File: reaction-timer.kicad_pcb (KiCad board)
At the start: 2 copper layers, 48 x 80 mm, 38 parts, among them IC1 4026, IC2 4026, IC3 4026, IC5 NE555P, IC6 NE555P, IC7 NE555P

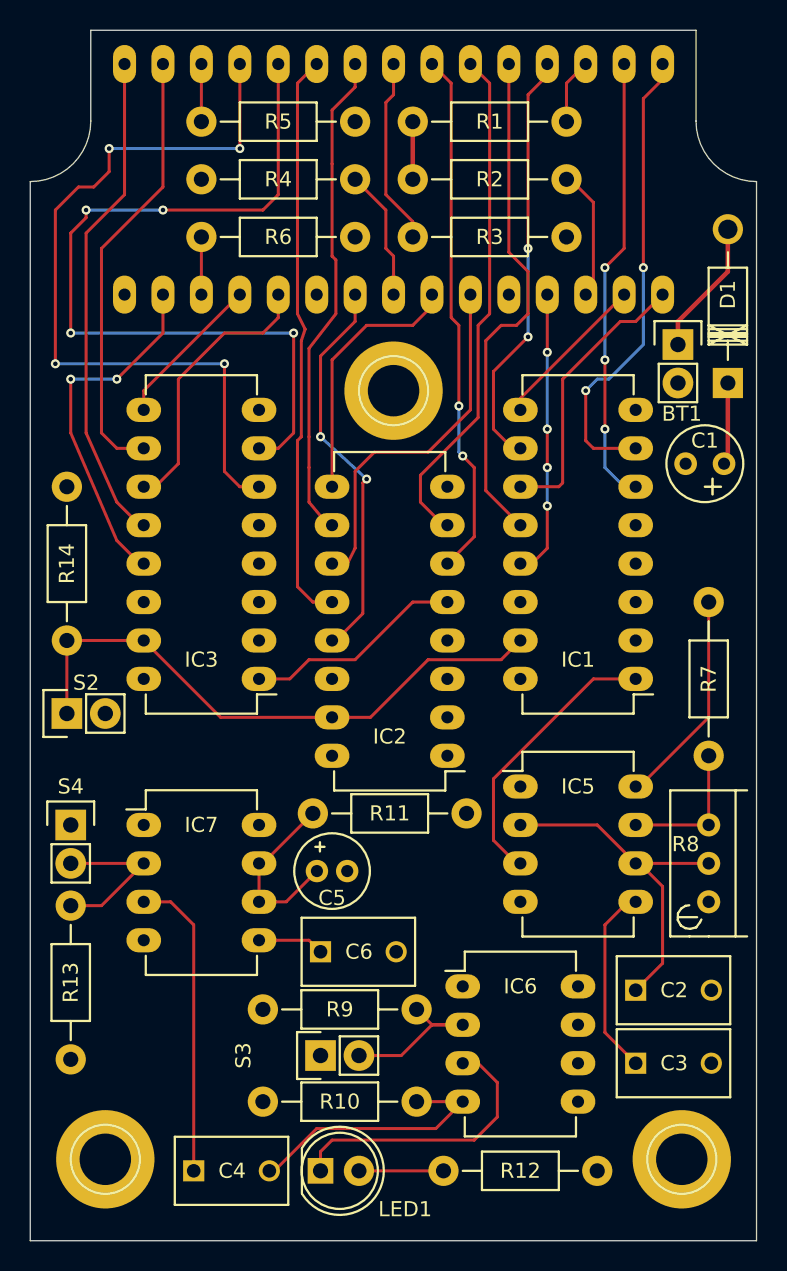
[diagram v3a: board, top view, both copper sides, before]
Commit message: Connect Vcc everywhere
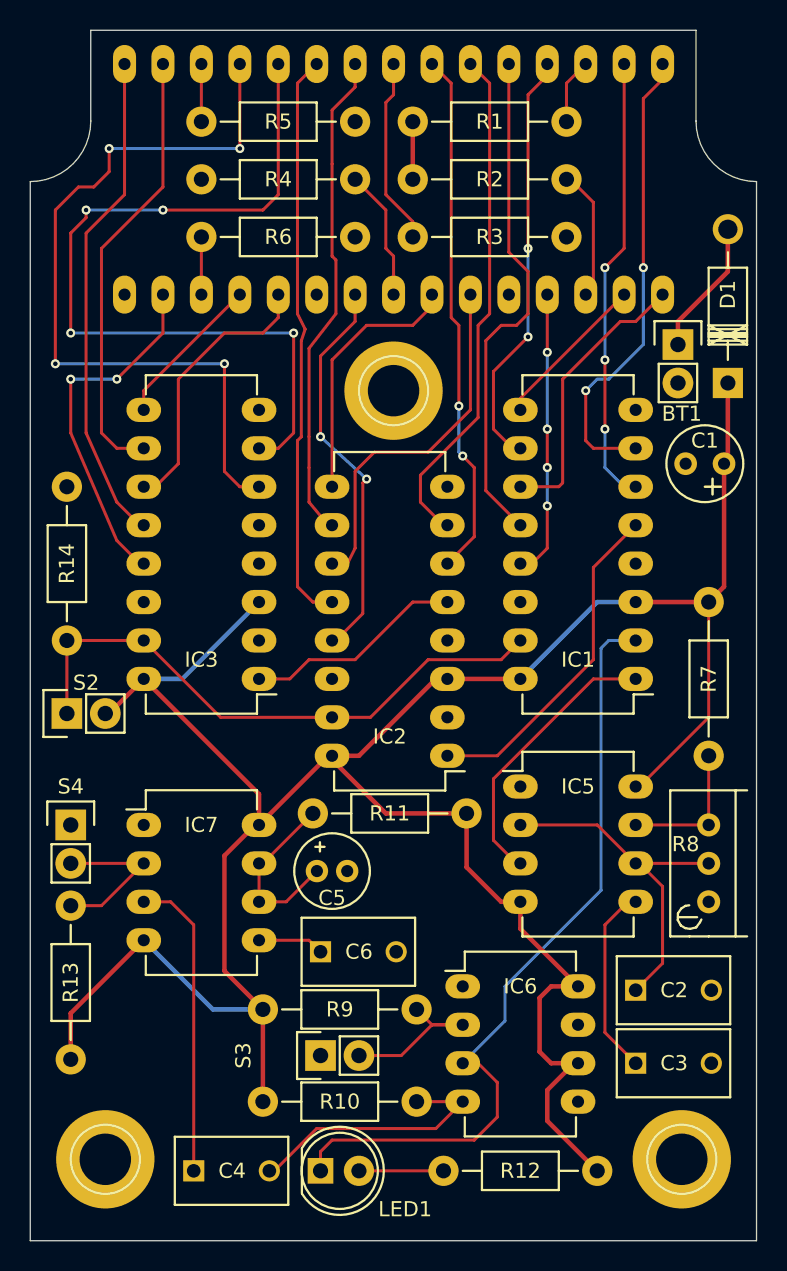
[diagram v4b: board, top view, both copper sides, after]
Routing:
- net Net-(C1-Pad1): track 19.8 -> 175.8 mm
- net Net-(IC1-Pad2): track 19.0 -> 52.7 mm
- net Net-(IC1-Pad5): track 0.00 -> 22.3 mm
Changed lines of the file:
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@@
   (general
     (links 104)
-    (no_connects 48)
+    (no_connects 28)
     (area 57.269499 61.269499 105.270501 141.270501)
     (thickness 1.6)
     (drawings 8)
-    (tracks 268)
+    (tracks 321)
     (zones 0)
     (modules 38)
@@
   (segment (start 100.076 82.042) (end 100.076 80.518) (width 0.3) (layer F.Cu) (net 31))
   (segment (start 82.55 67.31) (end 82.55 71.12) (width 0.3) (layer F.Cu) (net 32))
+  (segment (start 72.39 113.792) (end 72.136 113.792) (width 0.3) (layer F.Cu) (net 33) (status C00000))
+  (segment (start 72.136 113.792) (end 70.104 115.824) (width 0.3) (layer F.Cu) (net 33) (status 400000))
+  (segment (start 70.104 123.444) (end 72.644 125.984) (width 0.3) (layer F.Cu) (net 33) (status 800000))
+  (segment (start 70.104 115.824) (end 70.104 123.444) (width 0.3) (layer F.Cu) (net 33))
+  (segment (start 93.472 129.54) (end 93.218 129.54) (width 0.3) (layer F.Cu) (net 33) (status C00000))
+  (segment (start 93.218 129.54) (end 91.44 131.318) (width 0.3) (layer F.Cu) (net 33) (status 400000))
+  (segment (start 91.44 133.35) (end 94.742 136.652) (width 0.3) (layer F.Cu) (net 33) (status 800000))
+  (segment (start 91.44 131.318) (end 91.44 133.35) (width 0.3) (layer F.Cu) (net 33))
+  (segment (start 93.472 124.46) (end 91.694 124.46) (width 0.3) (layer F.Cu) (net 33) (status 400000))
+  (segment (start 91.694 129.54) (end 93.472 129.54) (width 0.3) (layer F.Cu) (net 33) (status 800000))
+  (segment (start 90.932 128.778) (end 91.694 129.54) (width 0.3) (layer F.Cu) (net 33))
+  (segment (start 90.932 125.222) (end 90.932 128.778) (width 0.3) (layer F.Cu) (net 33))
+  (segment (start 91.694 124.46) (end 90.932 125.222) (width 0.3) (layer F.Cu) (net 33))
+  (segment (start 89.662 118.872) (end 89.662 120.65) (width 0.3) (layer F.Cu) (net 33) (status 400000))
+  (segment (start 89.662 120.65) (end 93.472 124.46) (width 0.3) (layer F.Cu) (net 33) (status 800000))
+  (segment (start 89.662 118.872) (end 88.392 118.872) (width 0.3) (layer F.Cu) (net 33) (status 400000))
+  (segment (start 86.106 116.586) (end 86.106 113.03) (width 0.3) (layer F.Cu) (net 33) (status 800000))
+  (segment (start 88.392 118.872) (end 86.106 116.586) (width 0.3) (layer F.Cu) (net 33))
+  (segment (start 77.216 109.22) (end 77.216 109.474) (width 0.3) (layer F.Cu) (net 33) (status C00000))
+  (segment (start 77.216 109.474) (end 80.772 113.03) (width 0.3) (layer F.Cu) (net 33) (status 400000))
+  (segment (start 80.772 113.03) (end 86.106 113.03) (width 0.3) (layer F.Cu) (net 33) (status 800000))
+  (segment (start 72.644 125.984) (end 72.644 132.08) (width 0.3) (layer F.Cu) (net 33) (status C00000))
+  (segment (start 72.644 125.984) (end 69.342 125.984) (width 0.3) (layer B.Cu) (net 33) (status 400000))
+  (segment (start 69.342 125.984) (end 64.77 121.412) (width 0.3) (layer B.Cu) (net 33) (status 800000))
+  (segment (start 59.944 129.286) (end 59.944 126.238) (width 0.3) (layer F.Cu) (net 33) (status 400000))
+  (segment (start 59.944 126.238) (end 64.77 121.412) (width 0.3) (layer F.Cu) (net 33) (status 800000))
+  (segment (start 64.77 104.14) (end 67.31 104.14) (width 0.3) (layer B.Cu) (net 33) (status 400000))
+  (segment (start 67.31 104.14) (end 72.39 99.06) (width 0.3) (layer B.Cu) (net 33) (status 800000))
+  (segment (start 62.23 106.426) (end 62.484 106.426) (width 0.3) (layer F.Cu) (net 33) (status C00000))
+  (segment (start 62.484 106.426) (end 64.77 104.14) (width 0.3) (layer F.Cu) (net 33) (status C00000))
+  (segment (start 72.39 113.792) (end 72.39 111.76) (width 0.3) (layer F.Cu) (net 33) (status 400000))
+  (segment (start 72.39 111.76) (end 64.77 104.14) (width 0.3) (layer F.Cu) (net 33) (status 800000))
+  (segment (start 77.216 109.22) (end 76.962 109.22) (width 0.3) (layer F.Cu) (net 33) (status C00000))
+  (segment (start 76.962 109.22) (end 72.39 113.792) (width 0.3) (layer F.Cu) (net 33) (status C00000))
+  (segment (start 84.836 104.14) (end 84.074 104.14) (width 0.3) (layer F.Cu) (net 33) (status C00000))
+  (segment (start 84.074 104.14) (end 78.994 109.22) (width 0.3) (layer F.Cu) (net 33) (status 400000))
+  (segment (start 78.994 109.22) (end 77.216 109.22) (width 0.3) (layer F.Cu) (net 33) (status 800000))
+  (segment (start 89.662 104.14) (end 84.836 104.14) (width 0.3) (layer F.Cu) (net 33) (status C00000))
+  (segment (start 97.282 99.06) (end 94.742 99.06) (width 0.3) (layer B.Cu) (net 33) (status 400000))
+  (segment (start 94.742 99.06) (end 89.662 104.14) (width 0.3) (layer B.Cu) (net 33) (status 800000))
+  (segment (start 102.108 99.06) (end 97.282 99.06) (width 0.3) (layer F.Cu) (net 33))
+  (segment (start 103.124 89.916) (end 103.124 98.044) (width 0.3) (layer F.Cu) (net 33))
+  (segment (start 103.124 98.044) (end 102.108 99.06) (width 0.3) (layer F.Cu) (net 33))
   (segment (start 103.37546 84.582) (end 103.37546 89.66454) (width 0.3) (layer F.Cu) (net 33))
   (segment (start 102.108 106.68) (end 102.108 99.06) (width 0.2) (layer F.Cu) (net 33))
@@
   (segment (start 89.408 116.332) (end 87.884 114.808) (width 0.2) (layer F.Cu) (net 40))
   (segment (start 89.662 116.332) (end 89.408 116.332) (width 0.2) (layer F.Cu) (net 40))
+  (segment (start 97.282 101.6) (end 95.504 101.6) (width 0.2) (layer B.Cu) (net 41) (status 400000))
+  (segment (start 88.646 126.746) (end 85.852 129.54) (width 0.2) (layer B.Cu) (net 41) (status 800000))
+  (segment (start 88.646 124.46) (end 88.646 126.746) (width 0.2) (layer B.Cu) (net 41))
+  (segment (start 94.996 118.11) (end 88.646 124.46) (width 0.2) (layer B.Cu) (net 41))
+  (segment (start 94.996 102.108) (end 94.996 118.11) (width 0.2) (layer B.Cu) (net 41))
+  (segment (start 95.504 101.6) (end 94.996 102.108) (width 0.2) (layer B.Cu) (net 41))
   (segment (start 86.868 129.54) (end 85.852 129.54) (width 0.2) (layer F.Cu) (net 41))
   (segment (start 76.45266 135.38334) (end 77.216 134.62) (width 0.2) (layer F.Cu) (net 41))
@@
   (segment (start 88.138 130.81) (end 86.868 129.54) (width 0.2) (layer F.Cu) (net 41))
   (segment (start 76.45266 136.652) (end 76.45266 135.38334) (width 0.2) (layer F.Cu) (net 41))
+  (segment (start 84.836 109.22) (end 88.138 109.22) (width 0.2) (layer F.Cu) (net 42) (status 400000))
+  (segment (start 94.488 96.774) (end 97.282 93.98) (width 0.2) (layer F.Cu) (net 42) (status 800000))
+  (segment (start 94.488 102.87) (end 94.488 96.774) (width 0.2) (layer F.Cu) (net 42))
+  (segment (start 88.138 109.22) (end 94.488 102.87) (width 0.2) (layer F.Cu) (net 42))
   (segment (start 59.69 101.6) (end 59.69 106.426) (width 0.2) (layer F.Cu) (net 43))
   (segment (start 59.69 101.6) (end 64.77 101.6) (width 0.2) (layer F.Cu) (net 43))

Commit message: Ground fill
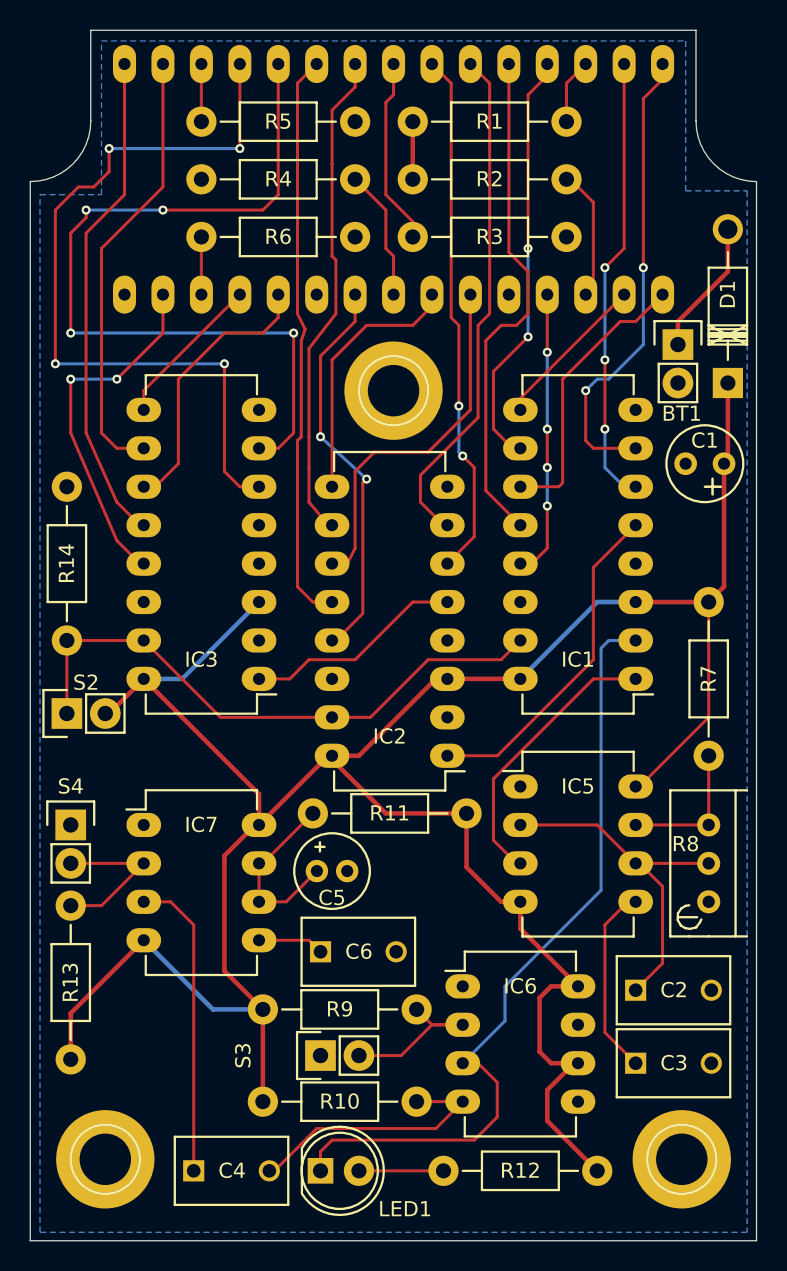
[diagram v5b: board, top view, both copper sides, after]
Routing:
- added copper zone on B.Cu, net GND
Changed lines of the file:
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@@
   (general
     (links 104)
-    (no_connects 28)
+    (no_connects 0)
     (area 57.269499 61.269499 105.270501 141.270501)
     (thickness 1.6)
@@
   (segment (start 59.944 119.126) (end 61.976 119.126) (width 0.2) (layer F.Cu) (net 49))
   (segment (start 78.99266 136.652) (end 84.582 136.652) (width 0.2) (layer F.Cu) (net 50))
+  (zone (net 32) (net_name GND) (layer B.Cu) (hatch edge 0.508)
+    (connect_pads (clearance 0.508))
+    (min_thickness 0.254)
+    (fill yes (arc_segments 16) (thermal_gap 0.508) (thermal_bridge_width 0.508))
+    (polygon
+      (pts
+        (xy 104.648 140.716) (xy 57.912 140.716) (xy 57.912 72.136) (xy 61.976 72.136) (xy 61.976 61.976)
+        (xy 100.584 61.976) (xy 100.584 71.882) (xy 104.648 71.882)
+      )
+    )
+  )
 )

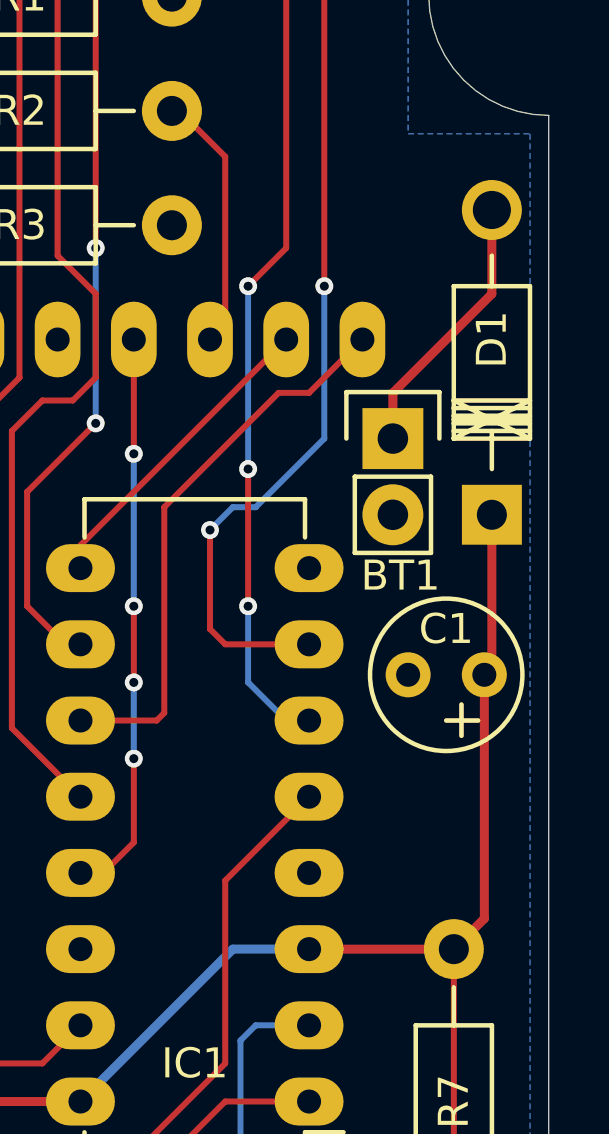
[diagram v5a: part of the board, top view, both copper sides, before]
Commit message: Move components to improve ground fill
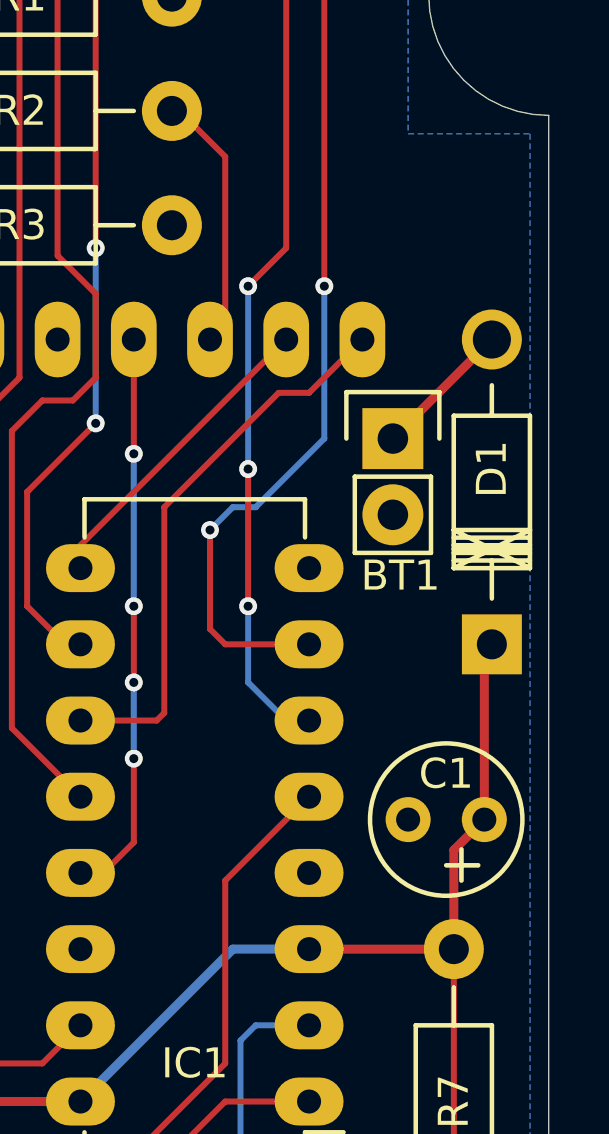
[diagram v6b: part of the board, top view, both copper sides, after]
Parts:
- moved C1 4.83 mm to (103.1, 94.7)
- moved D1 4.32 mm to (103.4, 88.9)
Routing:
- net Net-(C1-Pad1): track 175.8 -> 171.5 mm
- net +9V: track 8.99 -> 4.67 mm
